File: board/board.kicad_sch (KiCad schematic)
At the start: 26 parts, among them U1 ESP32-DevKitC, X1 ECS-2520MVLC-020.48-BN-TR

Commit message: worked feedback into layout
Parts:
- added R27, R28: 2k2, Resistor_SMD:R_0402_1005Metric, symbol Device:R_Small
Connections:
- net 3V3_SW: now also R27.1, R28.1
- net IMU/ASCK: now also R27.2
- net IMU/ASDA: now also R28.2
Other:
- note removed: "Mark default position of jumpers in layout"
- moved on the sheet: TP3, TP4
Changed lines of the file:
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@@
 (kicad_sch (version 20211123) (generator eeschema)
   (paper "A4")
+  (junction (at 172.72 55.88) (diameter 0) (color 0 0 0 0)
+  )
+  (junction (at 172.72 62.23) (diameter 0) (color 0 0 0 0)
+  )
   (junction (at 146.05 154.94) (diameter 0) (color 0 0 0 0)
   )
@@
   )
   (junction (at 162.56 154.94) (diameter 0) (color 0 0 0 0)
+  )
+  (junction (at 181.61 64.77) (diameter 0) (color 0 0 0 0)
   )
   (junction (at 162.56 111.76) (diameter 0) (color 0 0 0 0)
@@
     (stroke (width 0) (type default) (color 0 0 0 0))
   )
+  (wire (pts (xy 166.37 62.23) (xy 172.72 62.23))
+    (stroke (width 0) (type default) (color 0 0 0 0))
+  )
   (wire (pts (xy 80.01 152.4) (xy 106.68 152.4))
     (stroke (width 0) (type default) (color 0 0 0 0))
@@
     (stroke (width 0) (type default) (color 0 0 0 0))
   )
+  (wire (pts (xy 181.61 64.77) (xy 181.61 60.96))
+    (stroke (width 0) (type default) (color 0 0 0 0))
+  )
   (wire (pts (xy 137.16 148.59) (xy 137.16 154.94))
     (stroke (width 0) (type default) (color 0 0 0 0))
@@
     (stroke (width 0) (type default) (color 0 0 0 0))
   )
+  (wire (pts (xy 181.61 55.88) (xy 172.72 55.88))
+    (stroke (width 0) (type default) (color 0 0 0 0))
+  )
   (wire (pts (xy 224.79 142.24) (xy 228.6 142.24))
     (stroke (width 0) (type default) (color 0 0 0 0))
@@
     (stroke (width 0) (type default) (color 0 0 0 0))
   )
+  (wire (pts (xy 172.72 62.23) (xy 172.72 60.96))
+    (stroke (width 0) (type default) (color 0 0 0 0))
+  )
   (wire (pts (xy 101.6 172.72) (xy 106.68 172.72))
     (stroke (width 0) (type default) (color 0 0 0 0))
@@
     (stroke (width 0) (type default) (color 0 0 0 0))
   )
+  (wire (pts (xy 172.72 62.23) (xy 187.96 62.23))
+    (stroke (width 0) (type default) (color 0 0 0 0))
+  )
   (wire (pts (xy 214.63 119.38) (xy 228.6 119.38))
     (stroke (width 0) (type default) (color 0 0 0 0))
@@
     (stroke (width 0) (type default) (color 0 0 0 0))
   )
+  (wire (pts (xy 172.72 53.34) (xy 172.72 55.88))
+    (stroke (width 0) (type default) (color 0 0 0 0))
+  )
   (wire (pts (xy 96.52 55.88) (xy 100.33 55.88))
     (stroke (width 0) (type default) (color 0 0 0 0))
@@
     (stroke (width 0) (type default) (color 0 0 0 0))
   )
+  (wire (pts (xy 181.61 64.77) (xy 187.96 64.77))
+    (stroke (width 0) (type default) (color 0 0 0 0))
+  )
   (wire (pts (xy 96.52 63.5) (xy 100.33 63.5))
     (stroke (width 0) (type default) (color 0 0 0 0))
@@
     (stroke (width 0) (type default) (color 0 0 0 0))
   )
+  (wire (pts (xy 166.37 64.77) (xy 181.61 64.77))
+    (stroke (width 0) (type default) (color 0 0 0 0))
+  )
   (wire (pts (xy 146.05 143.51) (xy 146.05 137.16))
     (stroke (width 0) (type default) (color 0 0 0 0))
@@
   (wire (pts (xy 96.52 78.74) (xy 100.33 78.74))
     (stroke (width 0) (type default) (color 0 0 0 0))
-  )
-  (text "Mark default position of jumpers in layout" (at 137.16 26.67 0)
-    (effects (font (size 1.27 1.27)) (justify left bottom))
   )
   (label "I2C1_SCK" (at 147.32 87.63 180)
@@
   )
   (label "EKG_CS" (at 60.96 63.5 0)
+    (effects (font (size 1.27 1.27)) (justify left bottom))
+  )
+  (label "3V3_SW" (at 172.72 53.34 90)
     (effects (font (size 1.27 1.27)) (justify left bottom))
   )
@@
     (pin "2")
   )
-  (symbol (lib_id "Connector:TestPoint") (at 166.37 62.23 270) (unit 1)
-    (in_bom yes) (on_board yes)
-    (property "Reference" "TP3" (id 0) (at 179.07 62.23 90))
-    (property "Value" "ASCK" (id 1) (at 173.99 62.23 90))
-    (property "Footprint" "TestPoint:TestPoint_Pad_D1.0mm" (id 2) (at 166.37 67.31 0)
-      (effects (font (size 1.27 1.27)) hide)
-    )
-    (property "Datasheet" "~" (id 3) (at 166.37 67.31 0)
+  (symbol (lib_id "Device:R_Small") (at 181.61 58.42 0) (unit 1)
+    (in_bom yes) (on_board yes) (fields_autoplaced)
+    (property "Reference" "R28" (id 0) (at 184.15 57.1499 0)
+      (effects (font (size 1.27 1.27)) (justify left))
+    )
+    (property "Value" "2k2" (id 1) (at 184.15 59.6899 0)
+      (effects (font (size 1.27 1.27)) (justify left))
+    )
+    (property "Footprint" "Resistor_SMD:R_0402_1005Metric" (id 2) (at 181.61 58.42 0)
+      (effects (font (size 1.27 1.27)) hide)
+    )
+    (property "Datasheet" "~" (id 3) (at 181.61 58.42 0)
+      (effects (font (size 1.27 1.27)) hide)
+    )
+    (pin "1")
+    (pin "2")
+  )
+  (symbol (lib_id "Connector:TestPoint") (at 187.96 62.23 270) (unit 1)
+    (in_bom yes) (on_board yes)
+    (property "Reference" "TP3" (id 0) (at 200.66 62.23 90))
+    (property "Value" "ASCK" (id 1) (at 195.58 62.23 90))
+    (property "Footprint" "TestPoint:TestPoint_Pad_D1.0mm" (id 2) (at 187.96 67.31 0)
+      (effects (font (size 1.27 1.27)) hide)
+    )
+    (property "Datasheet" "~" (id 3) (at 187.96 67.31 0)
       (effects (font (size 1.27 1.27)) hide)
     )
@@
     (pin "1")
   )
-  (symbol (lib_id "Connector:TestPoint") (at 166.37 64.77 270) (unit 1)
-    (in_bom yes) (on_board yes)
-    (property "Reference" "TP4" (id 0) (at 179.07 64.77 90))
-    (property "Value" "ASDA" (id 1) (at 173.99 64.77 90))
-    (property "Footprint" "TestPoint:TestPoint_Pad_D1.0mm" (id 2) (at 166.37 69.85 0)
-      (effects (font (size 1.27 1.27)) hide)
-    )
-    (property "Datasheet" "~" (id 3) (at 166.37 69.85 0)
+  (symbol (lib_id "Connector:TestPoint") (at 187.96 64.77 270) (unit 1)
+    (in_bom yes) (on_board yes)
+    (property "Reference" "TP4" (id 0) (at 200.66 64.77 90))
+    (property "Value" "ASDA" (id 1) (at 195.58 64.77 90))
+    (property "Footprint" "TestPoint:TestPoint_Pad_D1.0mm" (id 2) (at 187.96 69.85 0)
+      (effects (font (size 1.27 1.27)) hide)
+    )
+    (property "Datasheet" "~" (id 3) (at 187.96 69.85 0)
       (effects (font (size 1.27 1.27)) hide)
     )
@@
     )
     (pin "1")
+  )
+  (symbol (lib_id "Device:R_Small") (at 172.72 58.42 0) (unit 1)
+    (in_bom yes) (on_board yes) (fields_autoplaced)
+    (property "Reference" "R27" (id 0) (at 175.26 57.1499 0)
+      (effects (font (size 1.27 1.27)) (justify left))
+    )
+    (property "Value" "2k2" (id 1) (at 175.26 59.6899 0)
+      (effects (font (size 1.27 1.27)) (justify left))
+    )
+    (property "Footprint" "Resistor_SMD:R_0402_1005Metric" (id 2) (at 172.72 58.42 0)
+      (effects (font (size 1.27 1.27)) hide)
+    )
+    (property "Datasheet" "~" (id 3) (at 172.72 58.42 0)
+      (effects (font (size 1.27 1.27)) hide)
+    )
+    (pin "1")
+    (pin "2")
   )
   (symbol (lib_id "Connector:TestPoint") (at 214.63 73.66 90) (unit 1)
@@
       (reference "#PWR0102") (unit 1) (value "+3V3") (footprint "")
     )
+    (path "/55fc5f4e-c0ad-4a73-bba2-08017d05c52a/88810b35-44bf-4587-9eb6-d4a4b5a13ea1"
+      (reference "#PWR0103") (unit 1) (value "GND") (footprint "")
+    )
     (path "/0133fba6-5aa6-4171-8a60-95549c0db33b/276cd6c7-4f5d-4216-ade6-7c20f595ba32"
       (reference "BT1") (unit 1) (value "5x AA / 6V 1200mAh") (footprint "Connector_PinHeader_2.54mm:PinHeader_1x02_P2.54mm_Vertical")
@@
       (reference "R26") (unit 1) (value "100k") (footprint "Resistor_SMD:R_0402_1005Metric")
     )
+    (path "/7df7a8af-01f4-4006-ac69-ff9eb0ceef28"
+      (reference "R27") (unit 1) (value "2k2") (footprint "Resistor_SMD:R_0402_1005Metric")
+    )
+    (path "/23e51d41-539e-40b0-acb1-729e3bdccb54"
+      (reference "R28") (unit 1) (value "2k2") (footprint "Resistor_SMD:R_0402_1005Metric")
+    )
+    (path "/55fc5f4e-c0ad-4a73-bba2-08017d05c52a/c702b59c-8d3f-4622-8b9c-4a7eaf8fba84"
+      (reference "R29") (unit 1) (value "100k") (footprint "Resistor_SMD:R_0402_1005Metric")
+    )
     (path "/55fc5f4e-c0ad-4a73-bba2-08017d05c52a/373dd208-ff72-4b71-b3ff-4847dea92ba1"

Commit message: did some minor stuff
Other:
- company: (none) -> Hochschule Pforzheim
- title: (none) -> eduSignal
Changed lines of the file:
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@@
 (kicad_sch (version 20211123) (generator eeschema)
   (paper "A4")
+  (title_block
+    (title "eduSignal")
+    (date "2022-07-14")
+    (rev "1")
+    (company "Hochschule Pforzheim")
+    (comment 1 "Patrick Hanner")
+    (comment 2 "Biosignal development board")
+  )
   (junction (at 172.72 55.88) (diameter 0) (color 0 0 0 0)
   )

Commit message: worked feedback into layout with dp
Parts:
- added TP27: RX, TestPoint:TestPoint_Pad_D1.0mm, symbol Connector:TestPoint
- added TP28: TX, TestPoint:TestPoint_Pad_D1.0mm, symbol Connector:TestPoint
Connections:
- net at U1.23 (TXD0): now also TP28.1
- net at U1.24 (RXD0): now also TP27.1
- no-connect marks 12 -> 10
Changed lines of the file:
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@@
   (no_connect (at 34.29 87.63))
   (no_connect (at 34.29 80.01))
-  (no_connect (at 60.96 83.82))
-  (no_connect (at 60.96 86.36))
   (no_connect (at 154.94 146.05))
   (no_connect (at 67.31 161.29))
@@
     (pin "9")
   )
+  (symbol (lib_id "Connector:TestPoint") (at 60.96 86.36 270) (unit 1)
+    (in_bom yes) (on_board yes)
+    (property "Reference" "TP28" (id 0) (at 73.66 86.36 90))
+    (property "Value" "TX" (id 1) (at 66.04 86.36 90)
+      (effects (font (size 1.27 1.27)) (justify left))
+    )
+    (property "Footprint" "TestPoint:TestPoint_Pad_D1.0mm" (id 2) (at 60.96 91.44 0)
+      (effects (font (size 1.27 1.27)) hide)
+    )
+    (property "Datasheet" "~" (id 3) (at 60.96 91.44 0)
+      (effects (font (size 1.27 1.27)) hide)
+    )
+    (pin "1")
+  )
   (symbol (lib_id "power:+3V3") (at 46.99 29.21 0) (unit 1)
     (in_bom yes) (on_board yes) (fields_autoplaced)
@@
     (pin "1")
     (pin "2")
+  )
+  (symbol (lib_id "Connector:TestPoint") (at 60.96 83.82 270) (unit 1)
+    (in_bom yes) (on_board yes)
+    (property "Reference" "TP27" (id 0) (at 73.66 83.82 90))
+    (property "Value" "RX" (id 1) (at 66.04 83.82 90)
+      (effects (font (size 1.27 1.27)) (justify left))
+    )
+    (property "Footprint" "TestPoint:TestPoint_Pad_D1.0mm" (id 2) (at 60.96 88.9 0)
+      (effects (font (size 1.27 1.27)) hide)
+    )
+    (property "Datasheet" "~" (id 3) (at 60.96 88.9 0)
+      (effects (font (size 1.27 1.27)) hide)
+    )
+    (pin "1")
   )
   (sheet (at 228.6 135.89) (size 12.7 11.43) (fields_autoplaced)
@@
       (reference "#PWR012") (unit 1) (value "GND") (footprint "")
     )
-    (path "/db6b8362-1493-4107-af7d-a8faca8bb053/b59172a8-bb63-4b8b-b5a0-5ee97f8f8b8e"
-      (reference "#PWR013") (unit 1) (value "+3V3") (footprint "")
-    )
     (path "/db6b8362-1493-4107-af7d-a8faca8bb053/b85c92b6-b689-426f-8425-c21cdee76e0f"
       (reference "#PWR014") (unit 1) (value "+5VA") (footprint "")
@@
       (reference "#PWR0103") (unit 1) (value "GND") (footprint "")
     )
+    (path "/db6b8362-1493-4107-af7d-a8faca8bb053/91a47725-5879-4993-a200-8231dec661e4"
+      (reference "#PWR0104") (unit 1) (value "+5VA") (footprint "")
+    )
+    (path "/0133fba6-5aa6-4171-8a60-95549c0db33b/5623fab3-1a5a-4a56-8338-e3362c22289d"
+      (reference "#PWR0105") (unit 1) (value "GND") (footprint "")
+    )
+    (path "/0133fba6-5aa6-4171-8a60-95549c0db33b/483397ea-f23d-4fc0-ac16-6af5e68fc91f"
+      (reference "#PWR0106") (unit 1) (value "GND") (footprint "")
+    )
     (path "/0133fba6-5aa6-4171-8a60-95549c0db33b/276cd6c7-4f5d-4216-ade6-7c20f595ba32"
       (reference "BT1") (unit 1) (value "5x AA / 6V 1200mAh") (footprint "Connector_PinHeader_2.54mm:PinHeader_1x02_P2.54mm_Vertical")
@@
       (reference "C50") (unit 1) (value "100n") (footprint "Capacitor_SMD:C_0402_1005Metric")
     )
+    (path "/0133fba6-5aa6-4171-8a60-95549c0db33b/b8c15e0f-2759-4d9e-9d3c-876dd7e890a8"
+      (reference "C51") (unit 1) (value "100n") (footprint "Capacitor_SMD:C_0402_1005Metric")
+    )
+    (path "/0133fba6-5aa6-4171-8a60-95549c0db33b/3d4b0cf5-2ded-45b7-988f-5f4ecb4de5fc"
+      (reference "C52") (unit 1) (value "100n") (footprint "Capacitor_SMD:C_0402_1005Metric")
+    )
     (path "/0133fba6-5aa6-4171-8a60-95549c0db33b/a887f37d-e480-4561-962e-f97c36c75a03"
       (reference "D1") (unit 1) (value "MMBZ15VALT1G") (footprint "Package_TO_SOT_SMD:SOT-23")
@@
       (reference "TP26") (unit 1) (value "PU2") (footprint "TestPoint:TestPoint_Pad_D1.0mm")
     )
+    (path "/f26cb318-07cc-4c67-ba18-2440c1b06691"
+      (reference "TP27") (unit 1) (value "RX") (footprint "TestPoint:TestPoint_Pad_D1.0mm")
+    )
+    (path "/85b4cc89-46fa-4af7-b26b-710647c4e01f"
+      (reference "TP28") (unit 1) (value "TX") (footprint "TestPoint:TestPoint_Pad_D1.0mm")
+    )
     (path "/2055161f-a421-43e7-aac1-c28f4d183a6b/ead0bbdd-06cd-41c0-9c2d-fff62be86454"

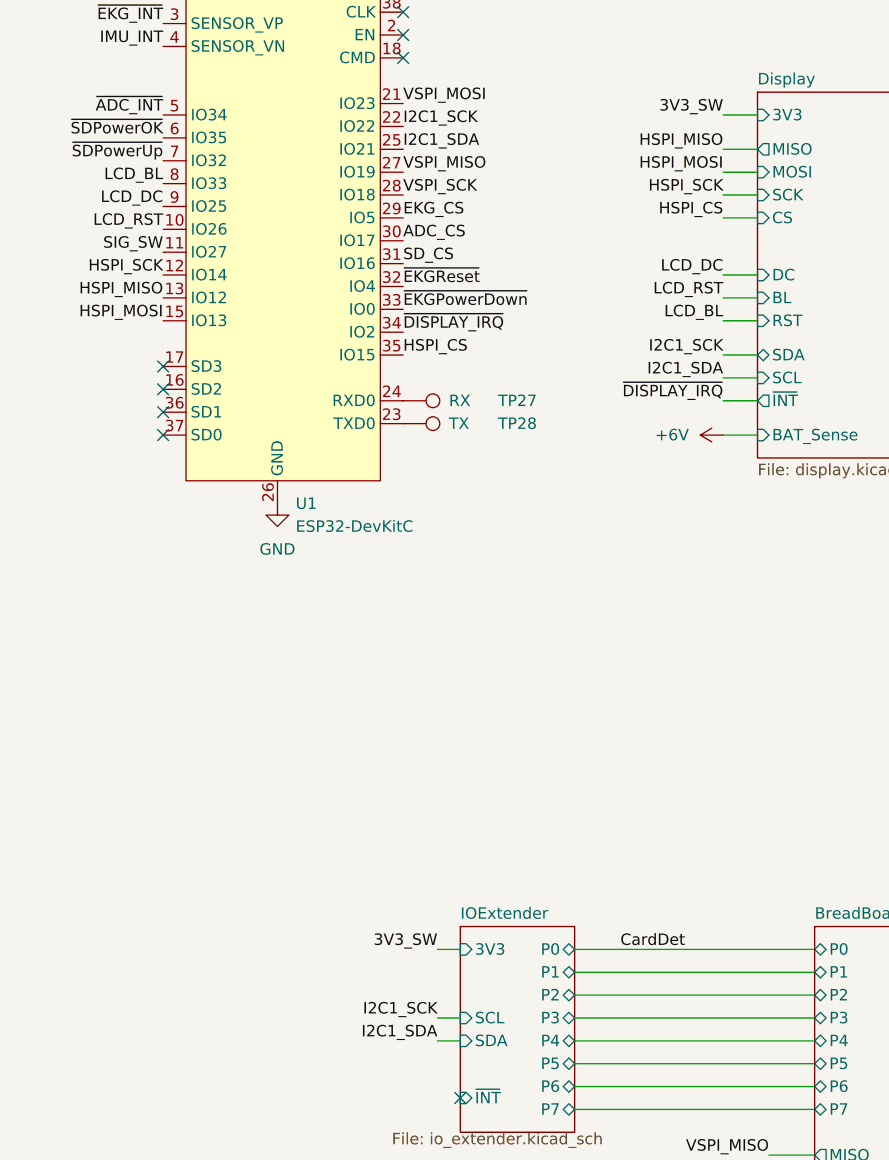
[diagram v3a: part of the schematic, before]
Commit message: fixed errors in schematic
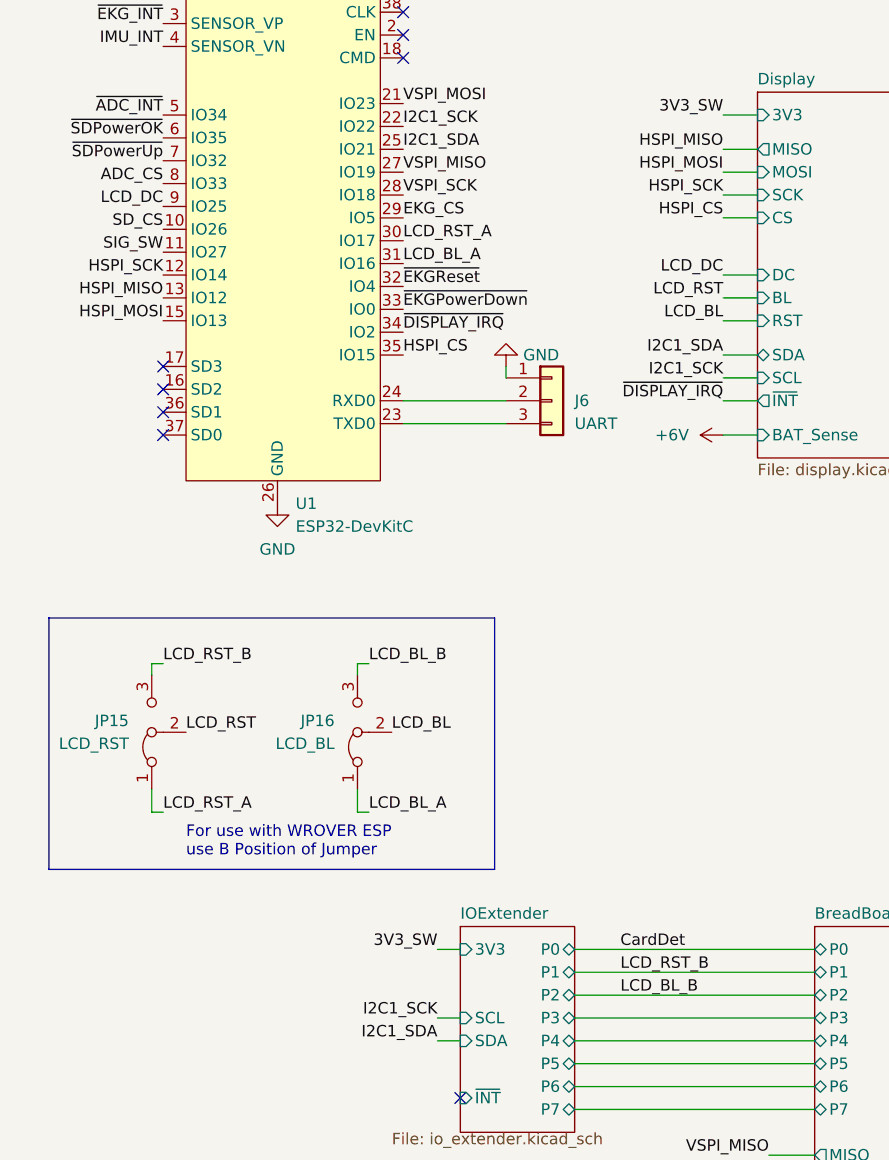
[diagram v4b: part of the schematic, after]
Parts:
- removed TP27: RX, TestPoint:TestPoint_Pad_D1.0mm, symbol Connector:TestPoint
- removed TP28: TX, TestPoint:TestPoint_Pad_D1.0mm, symbol Connector:TestPoint
- added J6: UART, Connector_PinHeader_2.54mm:PinHeader_1x03_P2.54mm_Vertical, symbol Connector_Generic:Conn_01x03
- added JP15: LCD_RST, Jumper:SolderJumper-3_P1.3mm_Bridged12_Pad1.0x1.5mm, symbol Jumper:Jumper_3_Bridged12
- added JP16: LCD_BL, Jumper:SolderJumper-3_P1.3mm_Bridged12_Pad1.0x1.5mm, symbol Jumper:Jumper_3_Bridged12
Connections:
- net ADC_CS: now also U1.8 (IO33); no longer U1.30 (IO17)
- net GND: now also J6.1 (Pin_1)
- net LCD_BL: now also JP16.2 (C); no longer U1.8 (IO33)
- net LCD_RST: now also JP15.2 (C); no longer U1.10 (IO26)
- net SD_CS: now also U1.10 (IO26); no longer U1.31 (IO16)
- net at U1.23 (TXD0): now also J6.3 (Pin_3)
- net at U1.24 (RXD0): now also J6.2 (Pin_2)
- new net LCD_BL_A: JP16.1 (A), U1.31 (IO16)
- new net LCD_BL_B: JP16.3 (B)
- new net LCD_RST_A: JP15.1 (A), U1.30 (IO17)
- new net LCD_RST_B: JP15.3 (B)
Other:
- note added: "For use with WROVER ESP use B Position of Jumper"

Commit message: Updated board
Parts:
- added R30, R31: 100k, Resistor_SMD:R_0402_1005Metric, symbol Device:R_Small
- JP15: value LCD_RST -> SD_OK
- JP16: value LCD_BL -> SD_UP
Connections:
- net +6V: now also R30.1
- net GND: now also R31.2
- net LCD_BL: now also U1.34 (IO2); no longer JP16.2 (C)
- net LCD_RST: now also U1.7 (IO32); no longer JP15.2 (C)
- net ~{DISPLAY_IRQ}: now also U1.6 (IO35); no longer U1.34 (IO2)
- net ~{SDPowerOK}: now also JP15.2 (C); no longer U1.6 (IO35)
- net ~{SDPowerUp}: now also JP16.2 (C); no longer U1.7 (IO32)
- net LCD_BL_A renamed SD_UP_A
- net LCD_BL_B renamed SD_UP_B
- net LCD_RST_A renamed SD_OK_A
- net LCD_RST_B renamed SD_OK_B
- new net Display/BAT_Sense: R30.2, R31.1
